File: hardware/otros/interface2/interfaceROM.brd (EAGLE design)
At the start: 73.6 x 29.4 mm, 15 parts, among them IC1 74HC174N, IC4 AM29F040S

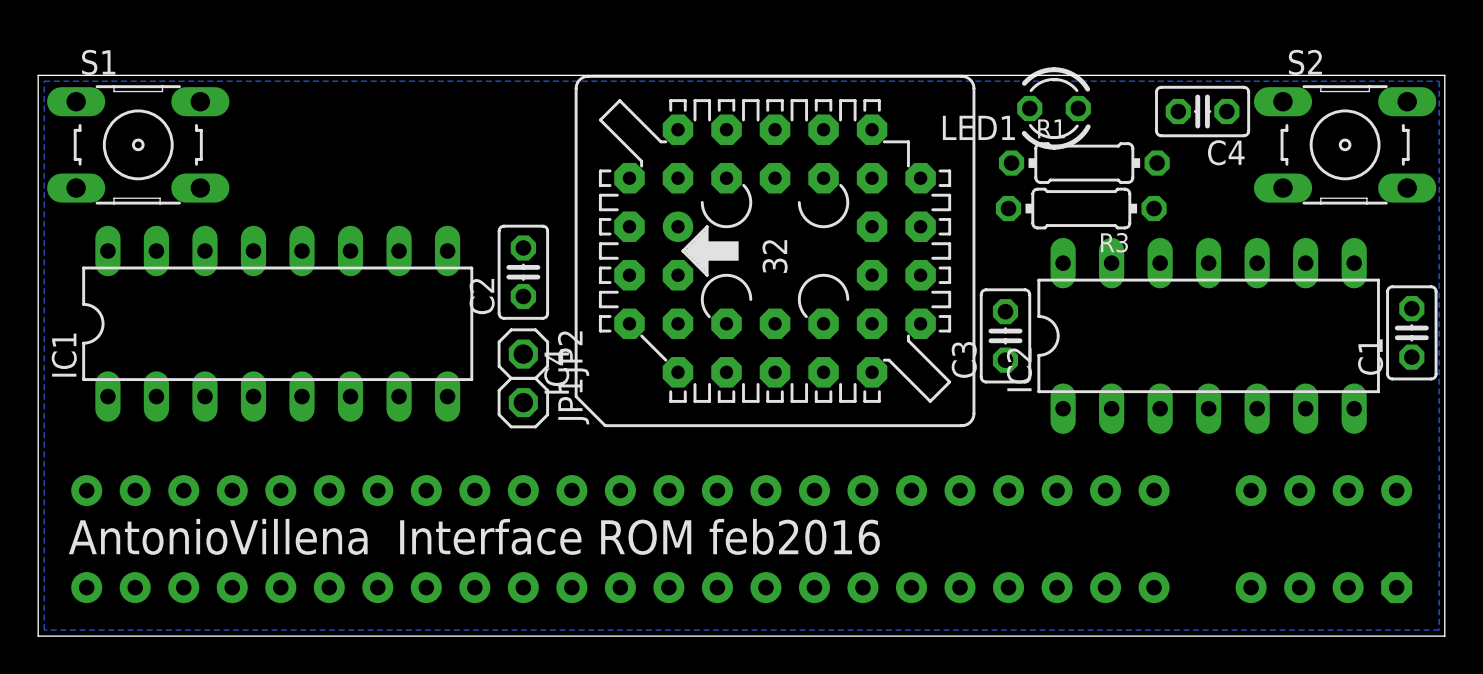
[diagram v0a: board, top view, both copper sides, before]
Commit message: 
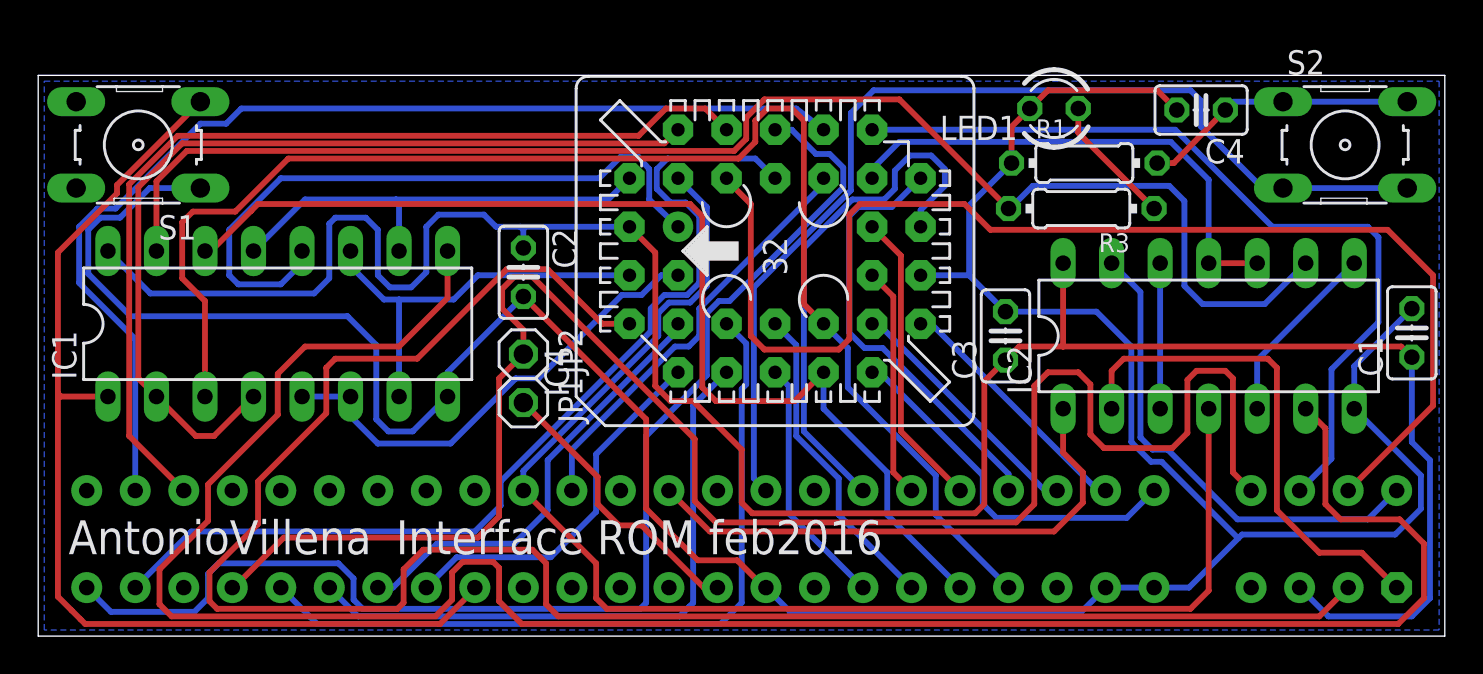
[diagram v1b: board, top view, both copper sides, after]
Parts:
- moved C4 0.11 mm to (60.9, 27.5)
- turned C2 to 270 degrees
- turned S1 to 180 degrees
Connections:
- net A14: now also IC2.2; no longer IC2.5
- net GND: no longer S1.2
- net MREQ: now also IC2.1; no longer IC2.4
- net N$2: now also IC2.6; no longer IC2.3
- net N$3: now also IC2.3; no longer IC2.6
- net N$4: now also IC2.5; no longer IC2.2
- net RESET: no longer S1.4
- net WR: now also IC2.4; no longer IC2.1
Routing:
- net GND: track 0.00 -> 157.1 mm
- net VCC: track 0.00 -> 124.6 mm
- net N$2: track 0.00 -> 113.3 mm
- net A12: track 0.00 -> 99.4 mm
- net ROMCS: track 0.00 -> 94.0 mm
- net LOCK: track 0.00 -> 75.2 mm
- net A0: track 0.00 -> 74.4 mm
- net WR: track 0.00 -> 71.0 mm
- net A13: track 0.00 -> 66.4 mm
- net A11: track 0.00 -> 65.2 mm
- net A1: track 0.00 -> 57.8 mm
- net A10: track 0.00 -> 56.9 mm
- net RESET: track 0.00 -> 54.9 mm
- net NMI: track 0.00 -> 54.7 mm
- net A9: track 0.00 -> 51.8 mm
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
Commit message: 
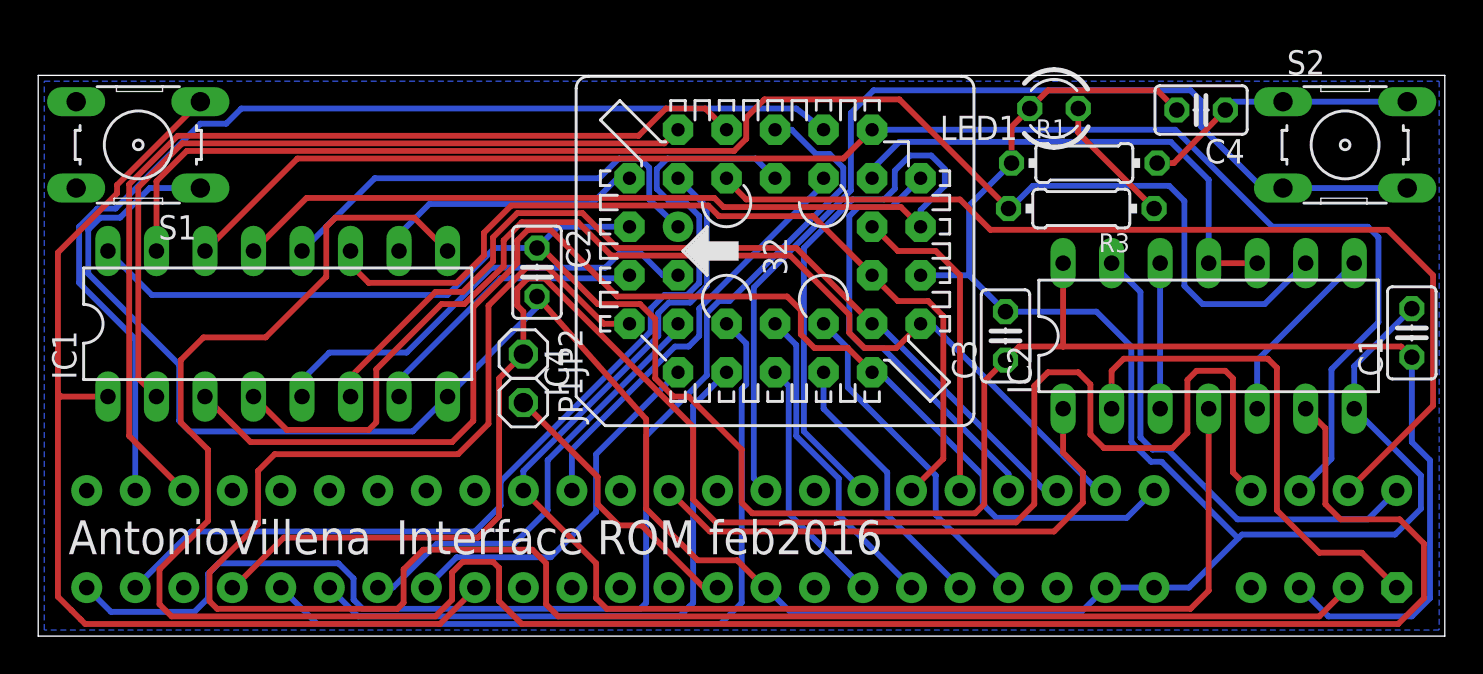
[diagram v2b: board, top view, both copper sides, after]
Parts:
- moved C2 0.71 mm to (26.1, 19.1)
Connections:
- net A0: no longer IC1.3
- net A1: no longer IC1.14
- net D0: now also IC1.3
- net D1: now also IC1.4
- net D2: now also IC1.6
- net D3: now also IC1.11
- net D4: now also IC1.13
- net D7: now also IC1.14
- net ROM14: no longer IC1.4
- net ROM15: no longer IC1.6
- net ROM16: no longer IC1.11
- net ROM17: no longer IC1.13
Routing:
- net A0: track 74.4 -> 17.8 mm
- net D0: track 19.4 -> 67.9 mm
- net D1: track 13.3 -> 59.7 mm
- net A1: track 57.8 -> 14.2 mm
- net D7: track 43.8 -> 81.4 mm
- net D4: track 27.8 -> 64.5 mm
- net D2: track 13.3 -> 48.3 mm
- net D3: track 12.1 -> 46.7 mm
- net A13: track 66.4 -> 52.3 mm
- net ROM18: track 35.0 -> 24.1 mm
- net ROM17: track 24.0 -> 14.2 mm
- net VCC: track 124.6 -> 117.6 mm
- net ROM14: track 47.6 -> 40.9 mm
- net ROM16: track 21.7 -> 15.2 mm
- net N$2: track 113.3 -> 119.5 mm
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
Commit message: Fix de la placa interface ROM, había que conectar ROMCS a VCC
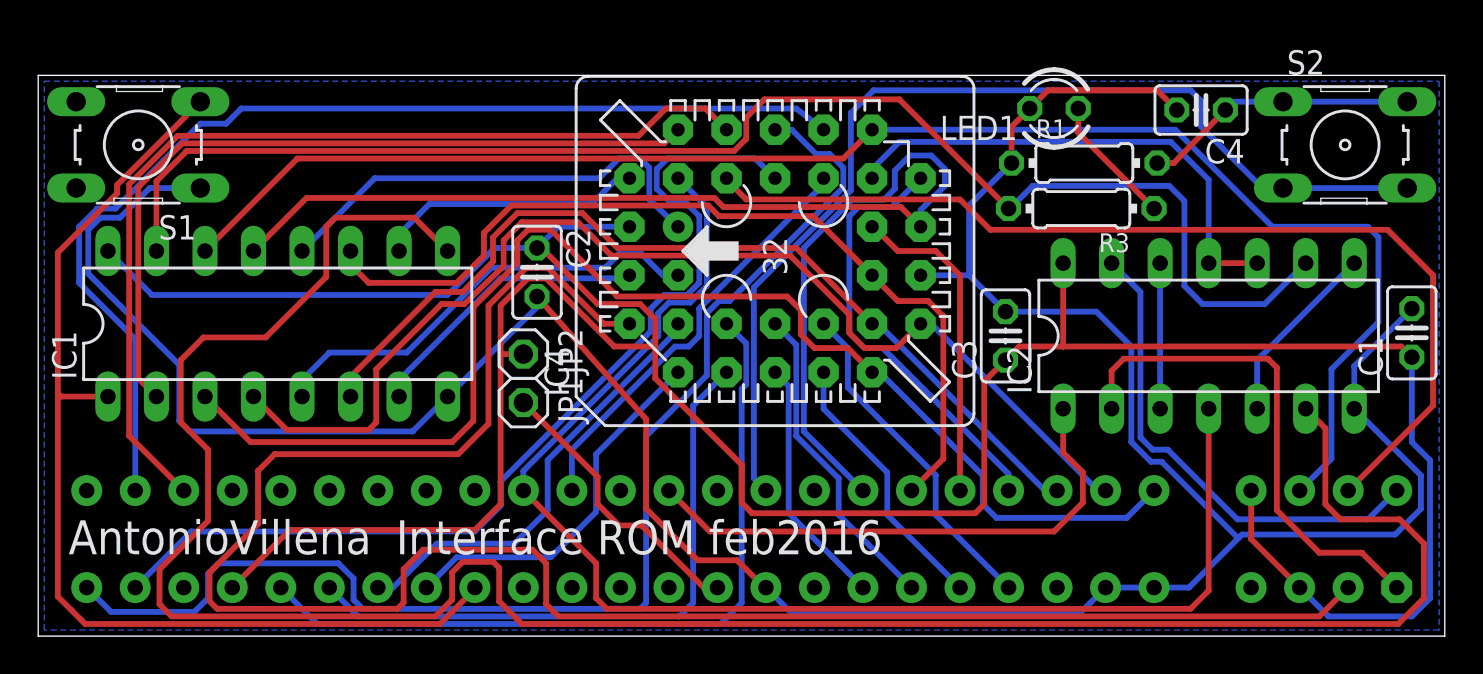
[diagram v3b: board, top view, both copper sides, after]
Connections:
- removed net ROMCS: JP2.1, U$3.A25, U$3.B4
- net VCC: now also JP2.1, U$3.A25, U$3.B4
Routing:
- net ROMCS: track 93.1 -> 0.00 mm
- net VCC: track 117.6 -> 160.9 mm
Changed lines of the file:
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@@
 <wire x1="51.355625" y1="15.160625" x2="50.64125" y2="14.44625" width="0.3048" layer="1"/>
 <wire x1="53.6575" y1="19.52625" x2="53.6575" y2="15.160625" width="0.3048" layer="1"/>
-<wire x1="32.305625" y1="13.49375" x2="33.258125" y2="12.54125" width="0.3048" layer="1"/>
-<wire x1="33.258125" y1="12.54125" x2="34.051875" y2="12.54125" width="0.3048" layer="1"/>
-<wire x1="34.051875" y1="12.54125" x2="36.83" y2="9.763125" width="0.3048" layer="1"/>
-<wire x1="36.83" y1="9.763125" x2="36.83" y2="6.985" width="0.3048" layer="1"/>
+<wire x1="32.305625" y1="13.49375" x2="36.83" y2="8.969375" width="0.3048" layer="1"/>
+<wire x1="36.83" y1="8.969375" x2="36.83" y2="6.985" width="0.3048" layer="1"/>
 <wire x1="36.83" y1="6.985" x2="37.385625" y2="6.429375" width="0.3048" layer="1"/>
 <wire x1="37.385625" y1="6.429375" x2="49.05375" y2="6.429375" width="0.3048" layer="1"/>
@@
 <wire x1="49.53" y1="6.905625" x2="49.53" y2="13.335" width="0.3048" layer="1"/>
 <wire x1="49.53" y1="13.335" x2="50.64125" y2="14.44625" width="0.3048" layer="1"/>
-<wire x1="32.305625" y1="13.49375" x2="32.305625" y2="16.589375" width="0.3048" layer="1"/>
+<wire x1="32.305625" y1="13.49375" x2="32.305625" y2="15.160625" width="0.3048" layer="1"/>
+<wire x1="32.305625" y1="15.160625" x2="32.305625" y2="16.589375" width="0.3048" layer="1"/>
 <wire x1="32.305625" y1="16.589375" x2="31.511875" y2="17.383125" width="0.3048" layer="1"/>
 <wire x1="31.511875" y1="17.383125" x2="29.289375" y2="17.383125" width="0.3048" layer="1"/>
@@
 <wire x1="21.43125" y1="17.859375" x2="5.953125" y2="17.859375" width="0.3048" layer="16"/>
 <wire x1="5.953125" y1="17.859375" x2="3.65125" y2="20.16125" width="0.3048" layer="16"/>
+<contactref element="U$3" pad="A25"/>
+<contactref element="U$3" pad="B4"/>
+<contactref element="JP2" pad="1"/>
+<wire x1="10.16" y1="2.54" x2="13.17625" y2="5.55625" width="0.3048" layer="1"/>
+<wire x1="13.17625" y1="5.55625" x2="22.86" y2="5.55625" width="0.3048" layer="1"/>
+<wire x1="22.86" y1="5.55625" x2="24.209375" y2="6.905625" width="0.3048" layer="1"/>
+<wire x1="24.209375" y1="6.905625" x2="24.209375" y2="14.843125" width="0.3048" layer="1"/>
+<wire x1="24.209375" y1="14.843125" x2="24.209375" y2="17.30375" width="0.3048" layer="1"/>
+<wire x1="24.209375" y1="17.30375" x2="25.638125" y2="18.7325" width="0.3048" layer="1"/>
+<wire x1="25.638125" y1="18.7325" x2="26.590625" y2="18.7325" width="0.3048" layer="1"/>
+<wire x1="26.590625" y1="18.7325" x2="30.1625" y2="15.160625" width="0.3048" layer="1"/>
+<wire x1="30.1625" y1="15.160625" x2="32.305625" y2="15.160625" width="0.3048" layer="1"/>
+<wire x1="25.4" y1="14.76375" x2="24.28875" y2="14.76375" width="0.3048" layer="1"/>
+<wire x1="24.28875" y1="14.76375" x2="24.209375" y2="14.843125" width="0.3048" layer="1"/>
+<wire x1="63.5" y1="7.62" x2="63.5" y2="5.08" width="0.3048" layer="1"/>
+<wire x1="63.5" y1="5.08" x2="66.04" y2="2.54" width="0.3048" layer="1"/>
 </signal>
 <signal name="GND">
@@
 <wire x1="34.528125" y1="3.96875" x2="31.829375" y2="6.6675" width="0.3048" layer="1"/>
 <wire x1="31.829375" y1="6.6675" x2="31.829375" y2="11.350625" width="0.3048" layer="1"/>
-<wire x1="31.829375" y1="11.350625" x2="26.114375" y2="17.78" width="0.3048" layer="1"/>
 <wire x1="8.48995" y1="23.4569" x2="5.83565" y2="23.4569" width="0.3048" layer="16"/>
 <wire x1="5.83565" y1="23.4569" x2="4.28625" y2="21.9075" width="0.3048" layer="16"/>
@@
 <wire x1="2.619375" y1="18.970625" x2="7.381875" y2="14.208125" width="0.3048" layer="16"/>
 <wire x1="7.381875" y1="14.208125" x2="7.381875" y2="11.27125" width="0.3048" layer="16"/>
+<wire x1="31.829375" y1="11.350625" x2="26.114375" y2="17.78" width="0.3048" layer="1"/>
 </signal>
 <signal name="D2">
@@
 <wire x1="2.460625" y1="0.635" x2="2.2225" y2="0.873125" width="0.3048" layer="1"/>
 </signal>
-<signal name="ROMCS">
-<contactref element="U$3" pad="A25"/>
-<contactref element="U$3" pad="B4"/>
-<contactref element="JP2" pad="1"/>
-<wire x1="10.16" y1="2.54" x2="10.239375" y2="2.54" width="0.3048" layer="1"/>
-<wire x1="10.239375" y1="2.54" x2="12.85875" y2="5.159375" width="0.3048" layer="1"/>
-<wire x1="12.85875" y1="5.159375" x2="23.01875" y2="5.159375" width="0.3048" layer="1"/>
-<wire x1="23.01875" y1="5.159375" x2="24.13" y2="6.270625" width="0.3048" layer="1"/>
-<wire x1="24.13" y1="6.270625" x2="24.13" y2="13.49375" width="0.3048" layer="1"/>
-<wire x1="24.13" y1="13.49375" x2="25.4" y2="14.76375" width="0.3048" layer="1"/>
-<wire x1="25.4" y1="14.76375" x2="25.4" y2="16.98625" width="0.3048" layer="1"/>
-<wire x1="34.29" y1="10.95375" x2="34.29" y2="7.14375" width="0.3048" layer="1"/>
-<wire x1="34.29" y1="7.14375" x2="35.480625" y2="5.953125" width="0.3048" layer="1"/>
-<wire x1="52.149375" y1="6.905625" x2="52.149375" y2="13.096875" width="0.3048" layer="1"/>
-<wire x1="62.5475" y1="13.49375" x2="62.5475" y2="8.5725" width="0.3048" layer="1"/>
-<wire x1="62.5475" y1="8.5725" x2="63.5" y2="7.62" width="0.3048" layer="1"/>
-<wire x1="62.5475" y1="13.49375" x2="62.150625" y2="13.890625" width="0.3048" layer="1"/>
-<wire x1="62.150625" y1="13.890625" x2="60.6425" y2="13.890625" width="0.3048" layer="1"/>
-<wire x1="60.6425" y1="13.890625" x2="60.16625" y2="13.414375" width="0.3048" layer="1"/>
-<wire x1="60.16625" y1="13.414375" x2="60.16625" y2="10.63625" width="0.3048" layer="1"/>
-<wire x1="60.16625" y1="10.63625" x2="59.3725" y2="9.8425" width="0.3048" layer="1"/>
-<wire x1="59.3725" y1="9.8425" x2="55.800625" y2="9.8425" width="0.3048" layer="1"/>
-<wire x1="55.800625" y1="9.8425" x2="55.08625" y2="10.556875" width="0.3048" layer="1"/>
-<wire x1="55.08625" y1="10.556875" x2="55.08625" y2="13.17625" width="0.3048" layer="1"/>
-<wire x1="55.08625" y1="13.17625" x2="54.45125" y2="13.81125" width="0.3048" layer="1"/>
-<wire x1="52.149375" y1="13.096875" x2="52.86375" y2="13.81125" width="0.3048" layer="1"/>
-<wire x1="52.86375" y1="13.81125" x2="54.45125" y2="13.81125" width="0.3048" layer="1"/>
-<wire x1="35.480625" y1="5.953125" x2="51.196875" y2="5.953125" width="0.3048" layer="1"/>
-<wire x1="51.196875" y1="5.953125" x2="52.149375" y2="6.905625" width="0.3048" layer="1"/>
-<wire x1="34.29" y1="10.95375" x2="26.51125" y2="18.7325" width="0.3048" layer="1"/>
-<wire x1="25.4" y1="16.98625" x2="25.0825" y2="17.30375" width="0.3048" layer="1"/>
-<wire x1="25.0825" y1="17.30375" x2="25.0825" y2="18.176875" width="0.3048" layer="1"/>
-<wire x1="25.0825" y1="18.176875" x2="25.638125" y2="18.7325" width="0.3048" layer="1"/>
-<wire x1="25.638125" y1="18.7325" x2="26.51125" y2="18.7325" width="0.3048" layer="1"/>
-</signal>
 <signal name="RD">
